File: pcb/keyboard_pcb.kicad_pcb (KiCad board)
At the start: 2 copper layers, 142.9 x 98.6 mm, 26 parts, among them J1 TRRS, K00 KEYSW, K01 KEYSW, K02 KEYSW, K03 KEYSW, K04 KEYSW, K05 KEYSW, K10 KEYSW, K11 KEYSW, K12 KEYSW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

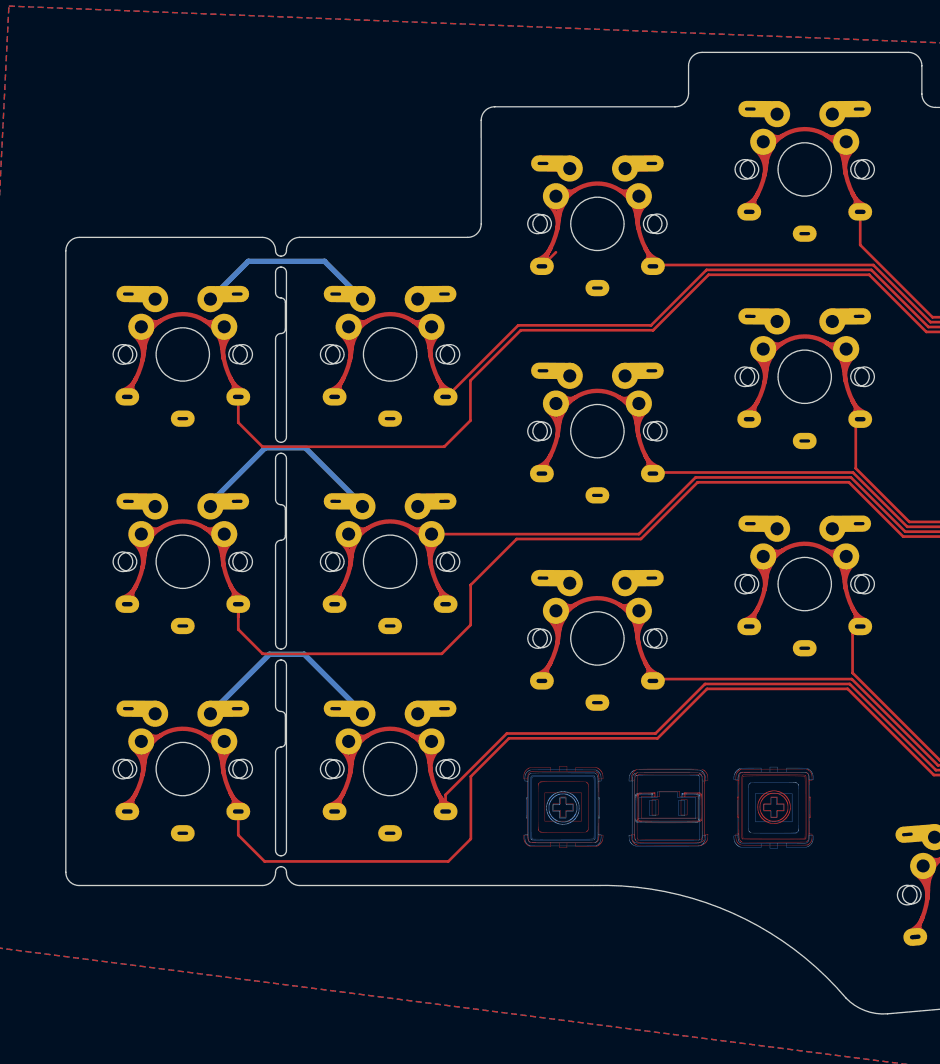
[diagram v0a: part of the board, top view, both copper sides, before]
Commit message: Truncated prototype created
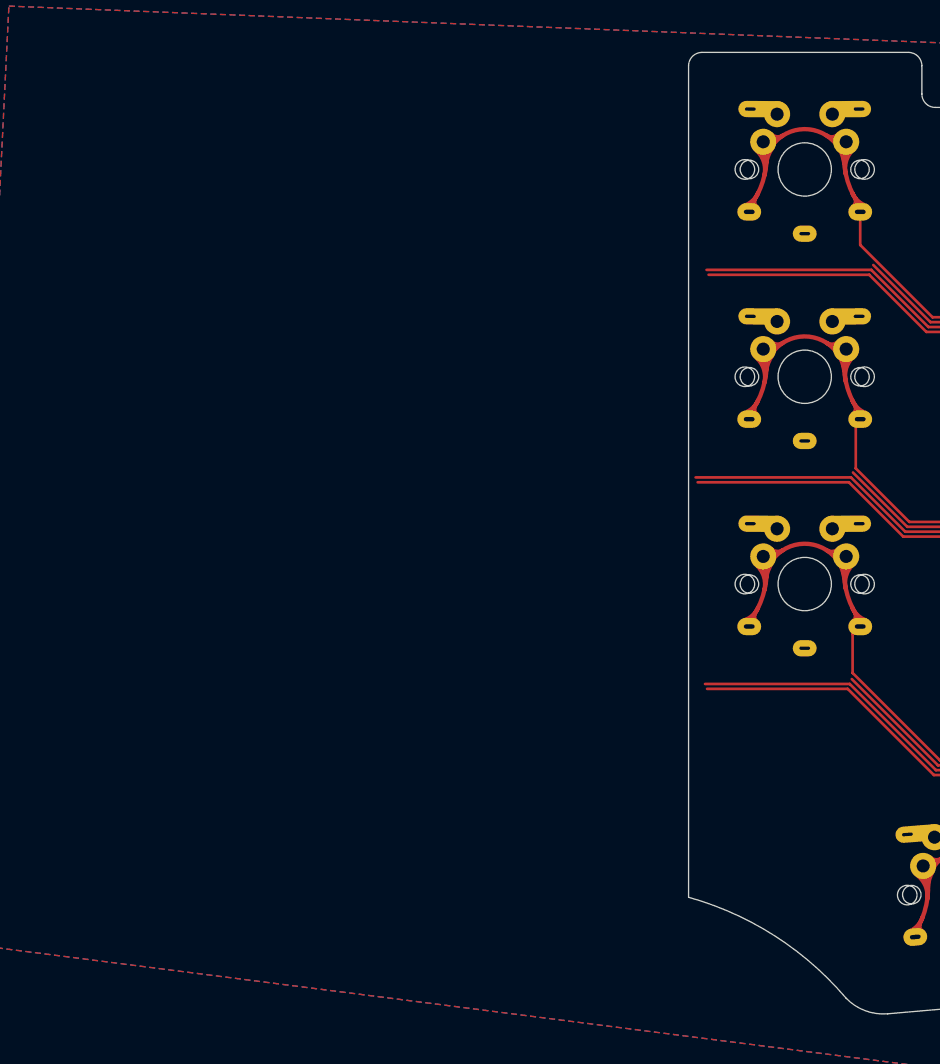
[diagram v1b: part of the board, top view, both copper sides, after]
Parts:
- removed the G*** at (113.2, 111.5)
- removed K00, K01, K02, K10, K11, K12, K20, K21, K22: KEYSW, Cantor_MasterKey:CherryMX_ChocV2_1u_DS
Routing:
- net /k20: track 170.2 -> 114.1 mm
- net /k10: track 141.2 -> 85.9 mm
- net /k00: track 169.9 -> 114.7 mm
- net GND: track 113.0 -> 59.5 mm
- net /k21: track 145.8 -> 116.2 mm
- net /k01: track 117.9 -> 89.3 mm
- net /k11: track 112.2 -> 85.0 mm
- net /k02: track 104.8 -> 82.6 mm
- net /k12: track 92.0 -> 73.6 mm
- net /k22: track 122.9 -> 104.6 mm
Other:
- board size 142.9 x 98.6 mm -> 85.6 x 98.6 mm
- board text removed: "JLCJLCJLCJLC"
